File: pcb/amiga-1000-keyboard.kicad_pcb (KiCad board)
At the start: 2 copper layers, 389.2 x 145 mm, 105 parts, among them SW1 ESC, SW10 F9, SW11 F10, SW12 HELP, SW13 `, SW14 1, SW15 2, SW16 3, SW17 4, SW18 5, SW19 6, SW2 F1, SW20 7, SW21 8, SW22 9, SW23 0, SW24 -, SW25 =, SW26 \, SW27 UP, SW28 TAB, SW29 Q, SW3 F2, SW30 W, SW31 E, SW32 R, SW33 T, SW34 Y, SW35 U, SW36 I, SW37 O, SW38 P, SW39 [, SW4 F3, SW40 ], SW41 RETURN, SW42 LEFT, SW43 CAPS LOCK, SW44 A, SW45 S, SW46 D, SW47 F, SW48 G, SW49 H, SW5 F4, SW50 J, SW51 K, SW52 L, SW53 ;, SW54 ', SW55 (RET) INTL, SW56 DEL, SW57 RIGHT, SW58 L SHIFT INTL, SW59 Z, SW6 F5, SW60 X, SW61 C, SW62 V, SW63 B, SW64 N, SW65 M, SW66 ,, SW67 ., SW68 /, SW69 SPACE, SW7 F6, SW70 BACKSPACE, SW71 DOWN, SW72 KP 9, SW73 KP 6, SW74 KP 3, SW75 KP ., SW76 KP 8, SW77 KP 5, SW78 KP 2, SW79 KP ENTER, SW8 F7, SW80 KP 7, SW81 KP 4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

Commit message: place the controller tab parts and tidy reference labels.
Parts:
- added C1: 1nF, Capacitor_THT:C_Disc_D5.0mm_W2.5mm_P5.00mm, F.Cu at (156.0, 44.5)
- added C2: 1nF, Capacitor_THT:C_Disc_D5.0mm_W2.5mm_P5.00mm, F.Cu at (156.0, 49.5)
- added C3: 1nF, Capacitor_THT:C_Disc_D5.0mm_W2.5mm_P5.00mm, F.Cu at (156.0, 54.0)
- added C4: 0.1uF, Capacitor_THT:C_Disc_D5.0mm_W2.5mm_P5.00mm, F.Cu at (180.2, 61.5)
- added C5: 1uF 25V tant, Capacitor_THT:CP_Radial_Tantal_D4.5mm_P2.50mm, F.Cu at (218.0, 47.0)
- added C6: 0.01uF, Capacitor_THT:C_Disc_D5.0mm_W2.5mm_P5.00mm, F.Cu at (195.0, 42.6)
- added C7: 0.1uF, Capacitor_THT:C_Disc_D5.0mm_W2.5mm_P5.00mm, F.Cu at (343.0, 51.0)
- added C8: 47uF 16V, Capacitor_THT:CP_Radial_D5.0mm_P2.00mm, F.Cu at (174.0, 45.0)
- added C9: 22pF, Capacitor_THT:C_Disc_D5.0mm_W2.5mm_P5.00mm, F.Cu at (281.9, 52.0)
- added D1: DIODE, Diode_THT:D_DO-35_SOD27_P7.62mm_Horizontal, F.Cu at (168.0, 52.3)
- added FB1: FB, Inductor_THT:L_Axial_L9.5mm_D4.0mm_P12.70mm_Horizontal_Fastron_SMCC, F.Cu at (139.7, 44.5)
- added FB2: FB, Inductor_THT:L_Axial_L9.5mm_D4.0mm_P12.70mm_Horizontal_Fastron_SMCC, F.Cu at (139.7, 49.5)
- added FB3: FB, Inductor_THT:L_Axial_L9.5mm_D4.0mm_P12.70mm_Horizontal_Fastron_SMCC, F.Cu at (139.7, 54.0)
- added J1: KEYBOARD, Connector_PinHeader_2.54mm:PinHeader_1x04_P2.54mm_Vertical, F.Cu at (131.0, 45.0)
- added Q1: NPN, amiga1000:TO-92_Inline_ECB, F.Cu at (115.5, 54.5)
- added R1: 150, Resistor_THT:R_Axial_DIN0207_L6.3mm_D2.5mm_P10.16mm_Horizontal, F.Cu at (102.0, 59.0)
- added R2: 510k, Resistor_THT:R_Axial_DIN0207_L6.3mm_D2.5mm_P10.16mm_Horizontal, F.Cu at (170.0, 58.0)
- added R3: 560k, Resistor_THT:R_Axial_DIN0207_L6.3mm_D2.5mm_P10.16mm_Horizontal, F.Cu at (186.0, 58.0)
- added U1: 6500/1, Package_DIP:DIP-40_W15.24mm, F.Cu at (339.7, 44.3)
- added U2: NE556, Package_DIP:DIP-14_W7.62mm, F.Cu at (200.1, 46.7)
- added Y1: 3.000MHz, Crystal:Crystal_HC49-U_Vertical, F.Cu at (277.0, 46.0)

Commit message: place the tab parts where the reproduction board has them.
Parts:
- moved R3 46.1 mm to (230.8, 47.1)
- moved C1 32.9 mm to (123.1, 45.9), turned to -90 degrees
- moved C2 28.1 mm to (128.1, 45.9), turned to -90 degrees
- moved C9 28.0 mm to (254.6, 45.6), turned to -90 degrees
- moved C6 24.5 mm to (219.5, 44.0), turned to -90 degrees
- moved C3 24.3 mm to (133.1, 45.9), turned to -90 degrees
- moved C4 20.2 mm to (168.5, 45.0), turned to -90 degrees
- moved Y1 17.3 mm to (259.7, 47.0)
- moved FB1 17.2 mm to (156.7, 46.4), turned to 180 degrees
- moved FB3 17.1 mm to (156.7, 55.6), turned to 180 degrees
- moved FB2 17.1 mm to (156.7, 51.0), turned to 180 degrees
- moved C8 15.8 mm to (189.5, 48.3), turned to 90 degrees
- moved U2 12.1 mm to (212.1, 48.5)
- moved D1 11.0 mm to (177.0, 58.6)
- moved R1 9.10 mm to (110.7, 61.6)
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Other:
- board text added: "Outline: caliper widths/depths; overall length 389.25 mm from scan - confirm by ruler. Hole and switch centres from a 200 dpi scan of a reproduction board (+/-0.15 mm)."
- board text removed: "CHECK: D2 polarity"
- board text removed: "CHECK: L SHIFT ISO"
- board text removed: "Outline: caliper widths/depths; overall length 389.25 mm from scan - confirm by ruler. Hole and switch centres from a 200 dpi scan of a reproduction board (+/-0.15 mm). CHECK: L SHIFT ISO assumed wired in parallel with L SHIFT - verify on a board."

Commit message: route the board with a ground pour on both layers.
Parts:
- H1, H2, H3, H4, H5, H6, H7, H8, H9: value Plate 3.8mm -> Plate GND; footprint amiga1000:MountingHole_3.8mm_Plate -> amiga1000:MountingHole_3.8mm_Plate_GND
- Q1: value NPN -> 2SC2021; footprint amiga1000:TO-92_Inline_ECB -> amiga1000:TO-92_Inline_Wide_ECB
- moved Q1 2.97 mm to (115.4, 56.6)
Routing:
- net /PD4: track 0.00 -> 515.0 mm, vias 0 -> 11
- net +5V: track 0.00 -> 504.3 mm, vias 0 -> 13
- net /PD3: track 0.00 -> 500.0 mm, vias 0 -> 7
- net /PD2: track 0.00 -> 458.5 mm, vias 0 -> 5
- net /PD1: track 0.00 -> 443.2 mm, vias 0 -> 5
- net /PD6: track 0.00 -> 420.3 mm, vias 0 -> 7
- net /PA3: track 0.00 -> 392.0 mm, vias 0 -> 3
- net /PA6: track 0.00 -> 390.2 mm, vias 0 -> 3
- net /PC5: track 0.00 -> 389.5 mm, vias 0 -> 5
- net /PA2: track 0.00 -> 385.6 mm, vias 0 -> 5
- net /PD5: track 0.00 -> 379.3 mm, vias 0 -> 3
- net /PA4: track 0.00 -> 377.8 mm, vias 0 -> 5
- net /PA5: track 0.00 -> 371.0 mm, vias 0 -> 3
- net /PD0: track 0.00 -> 364.9 mm, vias 0 -> 5
- net /PC6: track 0.00 -> 363.6 mm, vias 0 -> 5
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- added copper zone on B.Cu, net GND
- added copper zone on F.Cu, net GND

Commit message: turn the return switch round and fit sw55 as the dummy support housing.
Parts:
- turned SW41 to 270 degrees
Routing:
- net /PC1: track 250.7 -> 254.7 mm, vias 5 -> 6
- net /PA4: track 377.8 -> 377.9 mm, vias 5 -> 7
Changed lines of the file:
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@@
 			)
 		)
-		(property "Description" "International layouts only: extra key left of Return (original jumper J9)"
+		(property "Description" "US: dummy housing supporting the Return keycap. International: the extra key left of Return (original jumper J9)"
 			(at 0 0 0)
 			(layer "F.Fab")
@@
 			)
 		)
-		(property "Part" "Mitsumi standard mechanical Type 2 (KCT) keyswitch, salvaged"
+		(property "Part" "Dummy Mitsumi housing (one leg, no spring) supporting the Return keycap on US layouts; a real switch on international layouts"
 			(at 0 0 0)
 			(layer "F.Fab")
@@
 		(sheetname "/")
 		(sheetfile "amiga-1000-keyboard.kicad_sch")
-		(attr through_hole dnp)
+		(attr through_hole)
 		(duplicate_pad_numbers_are_jumpers no)
 		(fp_line
@@
 	(footprint "amiga1000:Mitsumi_A1000_Switch"
 		(layer "F.Cu")
-		(at 295.13 127.28 90)
+		(at 295.13 127.28 270)
 		(descr "Mitsumi standard mechanical Type 2 (KCT) keyswitch, Amiga 1000: 13.5 mm base, pins 9.04 mm apart and 4.75 mm right of the body centre; 1.2 mm holes (approx.)")
 		(property "Reference" "SW41"
-			(at -4.75 0 90)
+			(at -4.75 0 270)
 			(layer "F.SilkS")
 			(effects
@@
 		)
 		(property "Value" "RETURN"
-			(at 0 10.5 90)
+			(at 0 10.5 270)
 			(layer "F.Fab")
 			(effects
@@
 		)
 		(property "Datasheet" ""
-			(at 0 0 90)
+			(at 0 0 270)
 			(layer "F.Fab")
 			(hide yes)
@@
 		)
 		(property "Description" ""
-			(at 0 0 90)
+			(at 0 0 270)
 			(layer "F.Fab")
 			(hide yes)
@@
 		)
 		(property "Part" "Mitsumi standard mechanical Type 2 (KCT) keyswitch, salvaged"
-			(at 0 0 0)
+			(at 0 0 180)
 			(layer "F.Fab")
 			(hide yes)
@@
 		)
 		(pad "1" thru_hole circle
-			(at 0 -4.52 90)
+			(at 0 -4.52 270)
 			(size 2.3 2.3)
 			(drill 1.2)
@@
 		)
 		(pad "2" thru_hole circle
-			(at 0 4.52 90)
+			(at 0 4.52 270)
 			(size 2.3 2.3)
 			(drill 1.2)
@@
 			)
 		)
-		(property "Part" "1N4148 small-signal diode, DO-35"
+		(property "Part" "1N4148 small-signal diode, DO-35 (original: unmarked glass, yellow cathode band, likely a 1S1588)"
 			(at 0 0 0)
 			(layer "F.Fab")
@@
 	)
 	(segment
-		(start 318 52.5)
-		(end 317.9 52.6)
-		(width 0.25)
-		(layer "B.Cu")
-		(net "/PC0")
-	)
-	(segment
 		(start 282.7 137.9)
 		(end 281.2 136.4)
@@
 	)
 	(segment
-		(start 299.6 127.3)
-		(end 300.9 126)
-		(width 0.25)
-		(layer "F.Cu")
-		(net "/PA4")
-	)
-	(segment
 		(start 300.9 126)
 		(end 313.6 126)
@@
 	)
 	(segment
-		(start 299.6 127.3)
-		(end 299.6 123.5)
-		(width 0.25)
-		(layer "B.Cu")
-		(net "/PA4")
-	)
-	(segment
 		(start 319.5 62.4)
 		(end 319.5 68.3)
@@
 	)
 	(segment
-		(start 319.3 62.2)
-		(end 319.5 62.4)
-		(width 0.25)
-		(layer "B.Cu")
-		(net "/PA4")
-	)
-	(segment
 		(start 315.4 68.5)
 		(end 315.4 124.4)
@@
 	)
 	(segment
-		(start 315.5 68.4)
-		(end 315.4 68.5)
-		(width 0.25)
-		(layer "B.Cu")
-		(net "/PA4")
-	)
-	(segment
 		(start 175 48)
 		(end 189.2 48)
@@
 	)
 	(segment
-		(start 250.2 163)
-		(end 279.4 163)
-		(width 0.25)
-		(layer "F.Cu")
-		(net "/PC2")
-	)
-	(segment
 		(start 281.2 127.4)
 		(end 283.7 124.9)
@@
 	)
 	(segment
-		(start 166.8 165.3)
-		(end 247.9 165.3)
-		(width 0.25)
-		(layer "F.Cu")
-		(net "/PC2")
-	)
-	(segment
 		(start 276.2 108)
 		(end 276.2 107.4)
@@
 	)
 	(segment
-		(start 166.6 165.5)
-		(end 166.8 165.3)
-		(width 0.25)
-		(layer "F.Cu")
-		(net "/PC2")
-	)
-	(segment
 		(start 319 119.6)
 		(end 349.5 119.6)
@@
 	)
 	(segment
-		(start 247.9 165.3)
-		(end 250.2 163)
-		(width 0.25)
-		(layer "F.Cu")
-		(net "/PC2")
-	)
-	(segment
 		(start 283.7 124.9)
 		(end 299.3 124.9)
@@
 	)
 	(segment
-		(start 291.6 127.3)
-		(end 293.9 129.6)
-		(width 0.25)
-		(layer "F.Cu")
-		(net "/PC1")
-	)
-	(segment
 		(start 311.2 90.2)
 		(end 312.2 89.2)
@@
 	)
 	(segment
-		(start 290.6 127.3)
-		(end 291.6 127.3)
-		(width 0.25)
-		(layer "F.Cu")
-		(net "/PC1")
-	)
-	(segment
 		(start 311.2 90.2)
 		(end 311.3 90.2)
@@
 	)
 	(segment
-		(start 289.5 126.2)
-		(end 289.5 93.1)
-		(width 0.25)
-		(layer "B.Cu")
-		(net "/PC1")
-	)
-	(segment
 		(start 287.5 69.9)
 		(end 287.5 49.1)
@@
 	)
 	(segment
-		(start 290.6 127.3)
-		(end 289.5 126.2)
-		(width 0.25)
-		(layer "B.Cu")
-		(net "/PC1")
-	)
-	(segment
 		(start 133.6 98.3)
 		(end 114.6 98.3)
@@
 		(net "/PB6")
 	)
-	(segment
-		(start 83.4 165.4)
-		(end 83.6 165.2)
-		(width 0.25)
-		(layer "F.Cu")
-		(net "/PB6")
-	)
 	(via
 		(at 293 140.6)
@@
 	)
 	(embedded_fonts no)
+	(segment
+		(start 299.600000 123.500000)
+		(end 299.600000 125.250000)
+		(width 0.25)
+		(layer "B.Cu")
+		(net "/PA4")
+	)
+	(segment
+		(start 299.600000 125.250000)
+		(end 299.825000 125.475000)
+		(width 0.25)
+		(layer "B.Cu")
+		(net "/PA4")
+	)
+	(segment
+		(start 299.825000 125.475000)
+		(end 300.375000 125.475000)
+		(width 0.25)
+		(layer "F.Cu")
+		(net "/PA4")
+	)
+	(segment
+		(start 300.375000 125.475000)
+		(end 300.900000 126.000000)
+		(width 0.25)
+		(layer "F.Cu")
+		(net "/PA4")
+	)
+	(segment
+		(start 290.325000 123.500000)
+		(end 290.325000 126.300000)
+		(width 0.25)
+		(layer "B.Cu")
+		(net "/PA4")
+	)
+	(via
+		(at 299.825000 125.475000)
+		(size 0.8)
+		(drill 0.4)
+		(layers "F.Cu" "B.Cu")
+		(net "/PA4")
+	)
+	(via
+		(at 290.325000 123.500000)
+		(size 0.8)
+		(drill 0.4)
+		(layers "F.Cu" "B.Cu")
+		(net "/PA4")
+	)
+	(segment
+		(start 289.050000 128.825000)
+		(end 293.125000 128.825000)
+		(width 0.25)
+		(layer "F.Cu")
+		(net "/PC1")
+	)
+	(segment
+		(start 293.125000 128.825000)
+		(end 293.900000 129.600000)
+		(width 0.25)
+		(layer "F.Cu")
+		(net "/PC1")
+	)
+	(segment
+		(start 298.250000 129.600000)
+		(end 299.550000 128.300000)
+		(width 0.25)
+		(layer "F.Cu")
+		(net "/PC1")
+	)
+	(segment
+		(start 289.500000 93.100000)
+		(end 289.050000 93.550000)
+		(width 0.25)
+		(layer "B.Cu")
+		(net "/PC1")
+	)
+	(segment
+		(start 289.050000 93.550000)
+		(end 289.050000 128.825000)
+		(width 0.25)
+		(layer "B.Cu")
+		(net "/PC1")
+	)
+	(via
+		(at 289.050000 128.825000)
+		(size 0.8)
+		(drill 0.4)
+		(layers "F.Cu" "B.Cu")
+		(net "/PC1")
+	)
+	(segment
+		(start 166.800000 165.300000)
+		(end 169.100000 163.000000)
+		(width 0.25)
+		(layer "F.Cu")
+		(net "/PC2")
+	)
+	(segment
+		(start 169.100000 163.000000)
+		(end 279.400000 163.000000)
+		(width 0.25)
+		(layer "F.Cu")
+		(net "/PC2")
+	)
 )

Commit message: add version, source board number and repo url to the back silkscreen.
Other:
- board text added: "AMIGA 1000 KEYBOARD ${VERSION} Based on KCT-A89YC 56-7155B github.com/steveed/amiga-1000-keyboard-project"
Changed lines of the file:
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@@
 		(layer "Edge.Cuts")
+	)
+	(gr_text "AMIGA 1000 KEYBOARD ${VERSION}\nBased on KCT-A89YC 56-7155B\ngithub.com/steveed/amiga-1000-keyboard-project"
+		(at 300 180.6 0)
+		(layer "B.SilkS")
+		(effects
+			(font
+				(size 1.2 1.2)
+				(thickness 0.18)
+			)
+			(justify mirror)
+		)
 	)
 	(gr_text "Outline: caliper widths/depths; overall length 389.25 mm from scan - confirm by ruler.\nHole and switch centres from a 200 dpi scan of a reproduction board (+/-0.15 mm)."

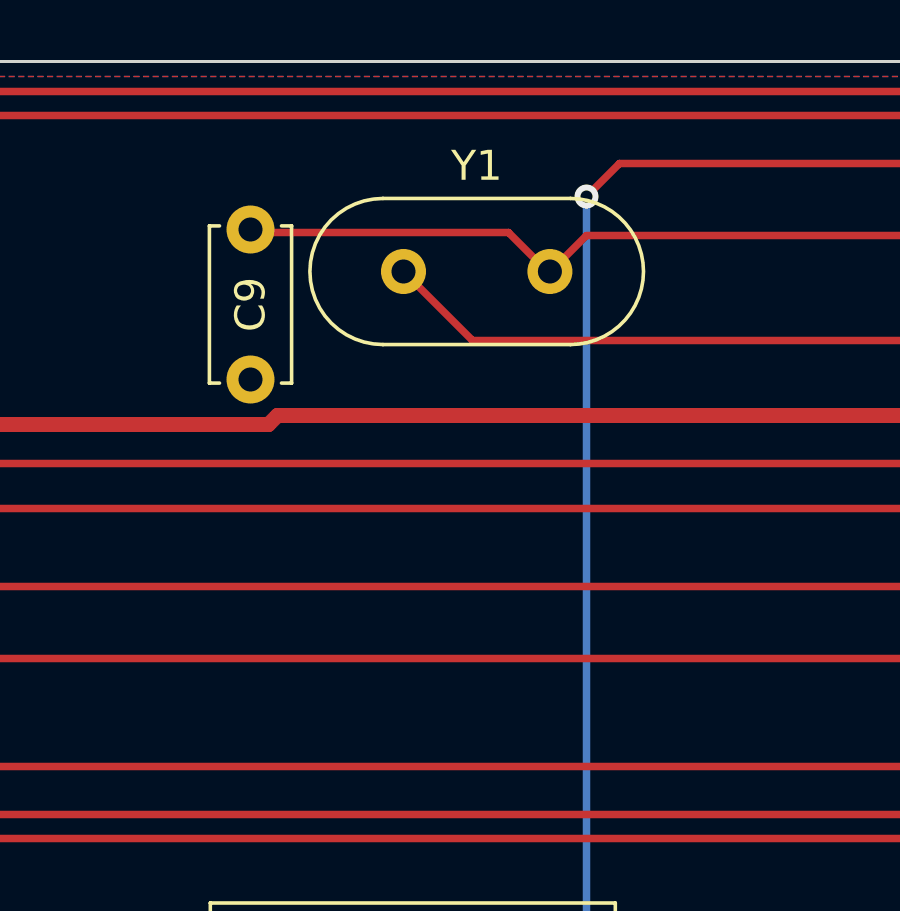
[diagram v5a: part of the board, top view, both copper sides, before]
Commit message: lay y1 flat on the board, can towards the keys, as on the original.
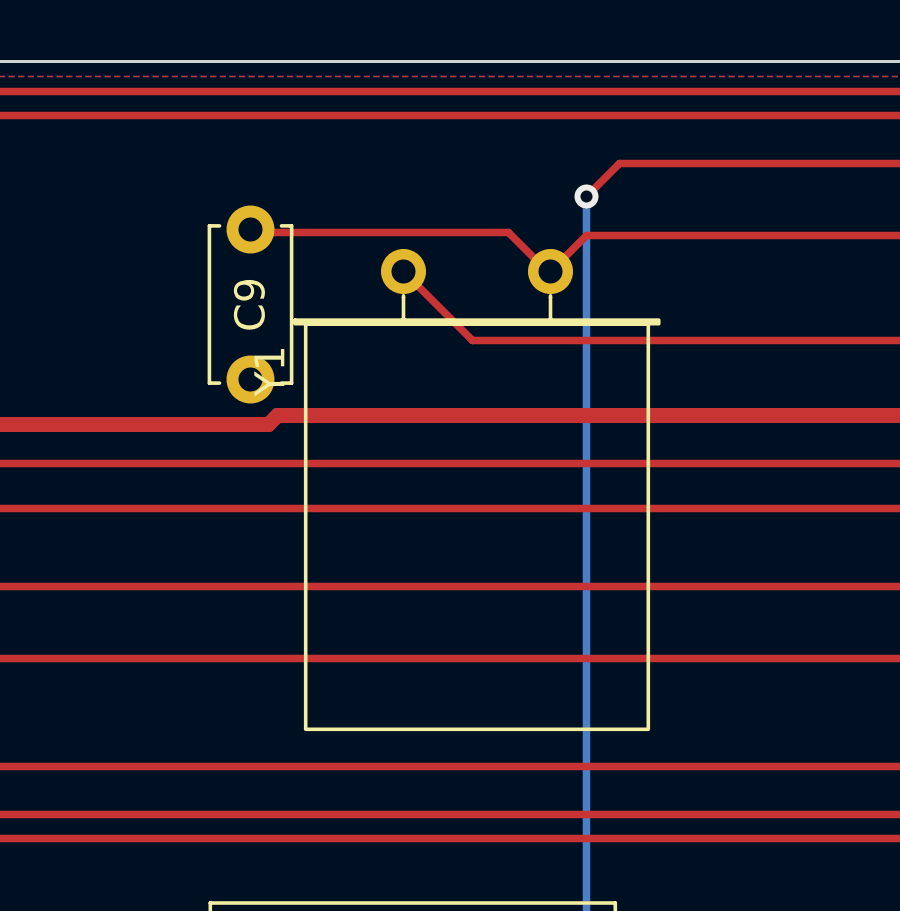
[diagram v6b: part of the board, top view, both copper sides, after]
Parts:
- Y1: footprint Crystal:Crystal_HC49-U_Vertical -> Crystal:Crystal_HC49-U_Horizontal
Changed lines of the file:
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@@
 		(embedded_fonts no)
 	)
-	(footprint "Crystal:Crystal_HC49-U_Vertical"
+	(footprint "Crystal:Crystal_HC49-U_Horizontal"
 		(layer "F.Cu")
 		(at 259.7 47)
-		(descr "HC-49/U, Crystal, http://5hertz.com/pdfs/04404_D.pdf")
+		(descr "HC-49/U, Crystal, length 13.0mm, width 10.9mm, THT, http://5hertz.com/pdfs/04404_D.pdf")
 		(property "Reference" "Y1"
-			(at 2.44 -3.52 180)
+			(at -4.435 3.3125 90)
 			(layer "F.SilkS")
 			(effects
@@
 		)
 		(property "Value" "3.000MHz"
-			(at 2.44 3.52 180)
+			(at 9.335 3.3125 90)
 			(layer "F.Fab")
 			(effects
@@
 		)
 		(property "Datasheet" ""
-			(at 0 0 180)
+			(at 0 0 0)
 			(layer "F.Fab")
 			(hide yes)
@@
 		)
 		(property "Description" ""
-			(at 0 0 180)
+			(at 0 0 0)
 			(layer "F.Fab")
 			(hide yes)
@@
 		)
 		(property "KiLib_Generator" "crystal_resonator_oscillator"
-			(at 0 0 180)
+			(at 0 0 0)
 			(layer "F.SilkS")
 			(hide yes)
@@
 			(effects
 				(font
-					(size 1 1)
-					(thickness 0.15)
-				)
-			)
-		)
-		(property ki_fp_filters "Crystal*")
+					(size 1.27 1.27)
+				)
+			)
+		)
 		(sheetname "/")
 		(sheetfile "amiga-1000-keyboard.kicad_sch")
@@
 		(duplicate_pad_numbers_are_jumpers no)
 		(fp_line
-			(start -0.685 -2.435)
-			(end 5.565 -2.435)
-			(stroke
-				(width 0.12)
-				(type solid)
-			)
-			(layer "F.SilkS")
-		)
-		(fp_line
-			(start 5.565 2.435)
-			(end -0.685 2.435)
-			(stroke
-				(width 0.12)
-				(type solid)
-			)
-			(layer "F.SilkS")
-		)
-		(fp_arc
-			(start -0.685 2.435)
-			(mid -3.12 0)
-			(end -0.685 -2.435)
-			(stroke
-				(width 0.12)
-				(type solid)
-			)
-			(layer "F.SilkS")
-		)
-		(fp_arc
-			(start 5.565 -2.435)
-			(mid 8 0)
-			(end 5.565 2.435)
-			(stroke
-				(width 0.12)
-				(type solid)
-			)
-			(layer "F.SilkS")
-		)
-		(fp_line
-			(start -0.68 -2.83)
-			(end 5.56 -2.83)
+			(start 0 0.87)
+			(end 0 0.81)
+			(stroke
+				(width 0.12)
+				(type solid)
+			)
+			(layer "F.SilkS")
+		)
+		(fp_line
+			(start 0 1.74)
+			(end 0 0.87)
+			(stroke
+				(width 0.12)
+				(type solid)
+			)
+			(layer "F.SilkS")
+		)
+		(fp_line
+			(start 4.9 0.87)
+			(end 4.9 0.81)
+			(stroke
+				(width 0.12)
+				(type solid)
+			)
+			(layer "F.SilkS")
+		)
+		(fp_line
+			(start 4.9 1.74)
+			(end 4.9 0.87)
+			(stroke
+				(width 0.12)
+				(type solid)
+			)
+			(layer "F.SilkS")
+		)
+		(fp_rect
+			(start -3.61 1.62)
+			(end 8.51 1.74)
+			(stroke
+				(width 0.12)
+				(type solid)
+			)
+			(fill no)
+			(layer "F.SilkS")
+		)
+		(fp_rect
+			(start -3.26 1.74)
+			(end 8.16 15.26)
+			(stroke
+				(width 0.12)
+				(type solid)
+			)
+			(fill no)
+			(layer "F.SilkS")
+		)
+		(fp_rect
+			(start -4.1 -1)
+			(end 9 16.25)
 			(stroke
 				(width 0.05)
 				(type solid)
 			)
+			(fill no)
 			(layer "F.CrtYd")
 		)
 		(fp_line
-			(start 5.56 2.83)
-			(end -0.68 2.83)
-			(stroke
-				(width 0.05)
-				(type solid)
-			)
-			(layer "F.CrtYd")
-		)
-		(fp_arc
-			(start -0.68 2.83)
-			(mid -3.51 0)
-			(end -0.68 -2.83)
-			(stroke
-				(width 0.05)
-				(type solid)
-			)
-			(layer "F.CrtYd")
-		)
-		(fp_arc
-			(start 5.56 -2.83)
-			(mid 8.39 0)
-			(end 5.56 2.83)
-			(stroke
-				(width 0.05)
-				(type solid)
-			)
-			(layer "F.CrtYd")
-		)
-		(fp_line
-			(start -0.685 -2.325)
-			(end 5.565 -2.325)
-			(stroke
-				(width 0.1)
-				(type solid)
-			)
-			(layer "F.Fab")
-		)
-		(fp_line
-			(start 5.565 2.325)
-			(end -0.685 2.325)
-			(stroke
-				(width 0.1)
-				(type solid)
-			)
-			(layer "F.Fab")
-		)
-		(fp_arc
-			(start -0.685 2.325)
-			(mid -3.01 0)
-			(end -0.685 -2.325)
-			(stroke
-				(width 0.1)
-				(type solid)
-			)
-			(layer "F.Fab")
-		)
-		(fp_arc
-			(start 5.565 -2.325)
-			(mid 7.89 0)
-			(end 5.565 2.325)
-			(stroke
-				(width 0.1)
-				(type solid)
-			)
+			(start 0 1)
+			(end 0 0)
+			(stroke
+				(width 0.1)
+				(type solid)
+			)
+			(layer "F.Fab")
+		)
+		(fp_line
+			(start 0 2)
+			(end 0 1)
+			(stroke
+				(width 0.1)
+				(type solid)
+			)
+			(layer "F.Fab")
+		)
+		(fp_line
+			(start 4.9 1)
+			(end 4.9 0)
+			(stroke
+				(width 0.1)
+				(type solid)
+			)
+			(layer "F.Fab")
+		)
+		(fp_line
+			(start 4.9 2)
+			(end 4.9 1)
+			(stroke
+				(width 0.1)
+				(type solid)
+			)
+			(layer "F.Fab")
+		)
+		(fp_rect
+			(start -3.35 1.9)
+			(end 8.25 2)
+			(stroke
+				(width 0.1)
+				(type solid)
+			)
+			(fill no)
+			(layer "F.Fab")
+		)
+		(fp_rect
+			(start -3 2)
+			(end 7.9 15)
+			(stroke
+				(width 0.1)
+				(type solid)
+			)
+			(fill no)
 			(layer "F.Fab")
 		)
 		(fp_text user "${REFERENCE}"
-			(at 2.44 0 180)
+			(at 2.45 9.35 90)
 			(layer "F.Fab")
 			(effects
@@
 			(remove_unused_layers no)
 			(net "/XTLI")
-			(pinfunction "1_1")
-			(pintype "passive")
 		)
 		(pad "2" thru_hole circle
-			(at 4.88 0)
+			(at 4.9 0)
 			(size 1.5 1.5)
 			(drill 0.8)
@@
 			(remove_unused_layers no)
 			(net "/XTLO")
-			(pinfunction "2_2")
-			(pintype "passive")
 		)
 		(embedded_fonts no)
-		(model "${KICAD10_3DMODEL_DIR}/Crystal.3dshapes/Crystal_HC49-U_Vertical.step"
+		(model "${KICAD10_3DMODEL_DIR}/Crystal.3dshapes/Crystal_HC49-U_Horizontal.step"
 			(offset
 				(xyz 0 0 0)
